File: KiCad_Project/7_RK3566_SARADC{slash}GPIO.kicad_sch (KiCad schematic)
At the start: 9 parts

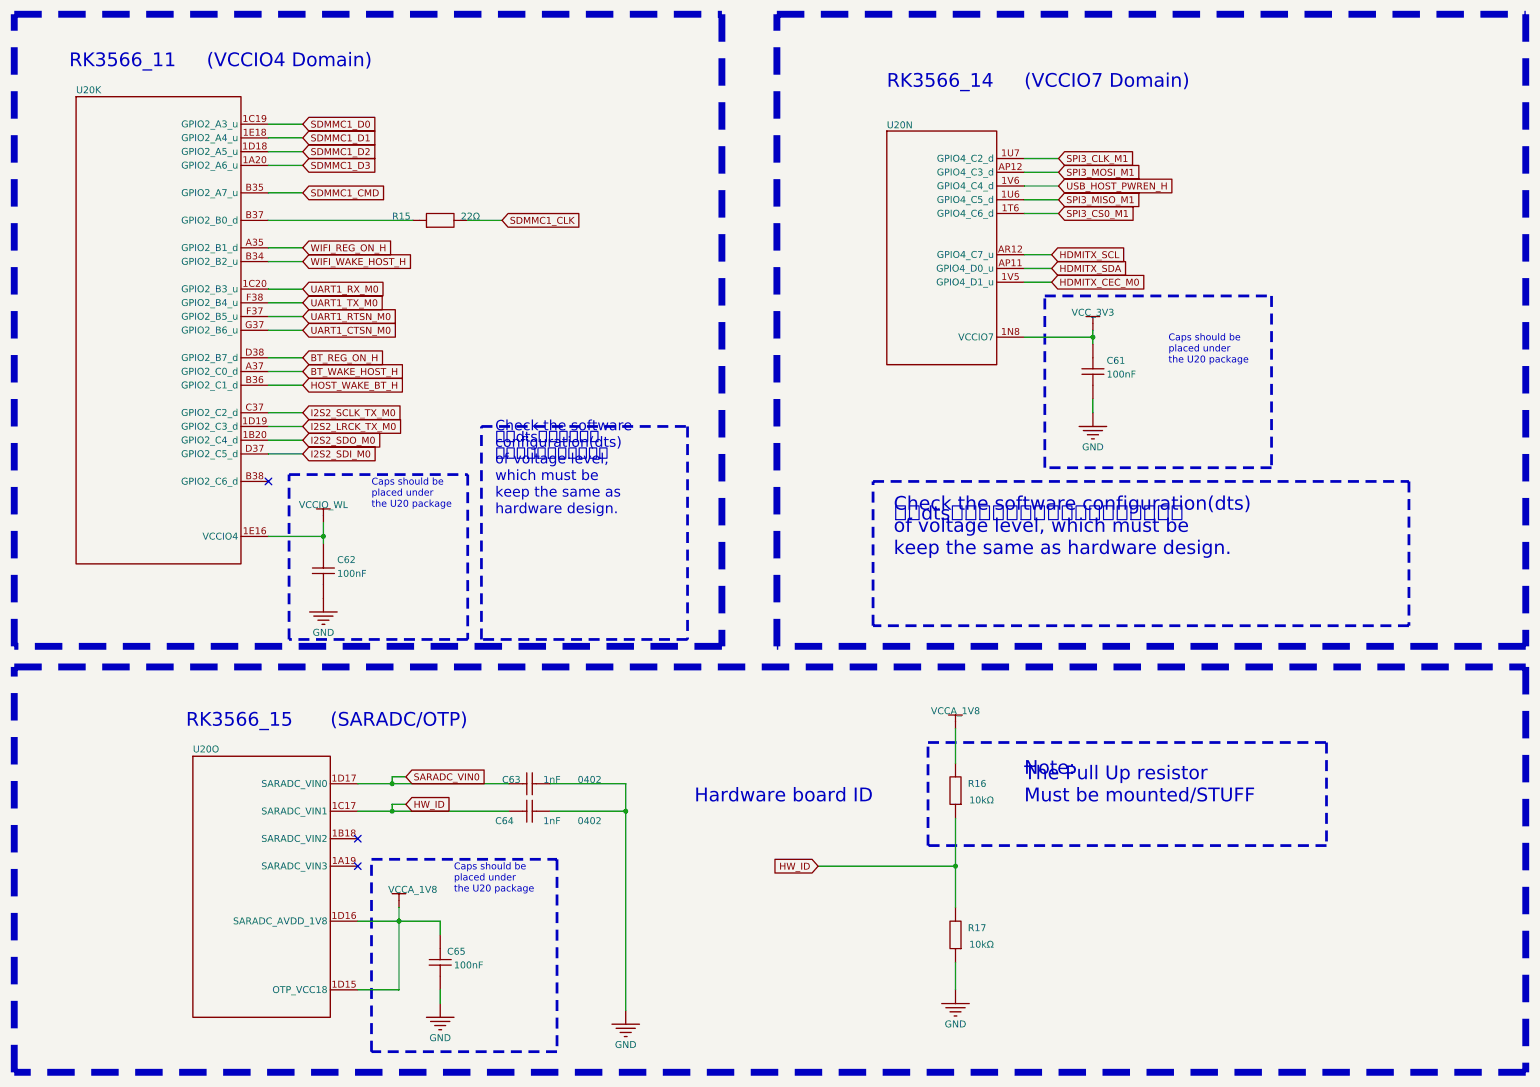
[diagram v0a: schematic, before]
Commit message: Update additional PCBs
Add WIFI PCB to get best antenna
Add Display Debbugger to get interface pinout
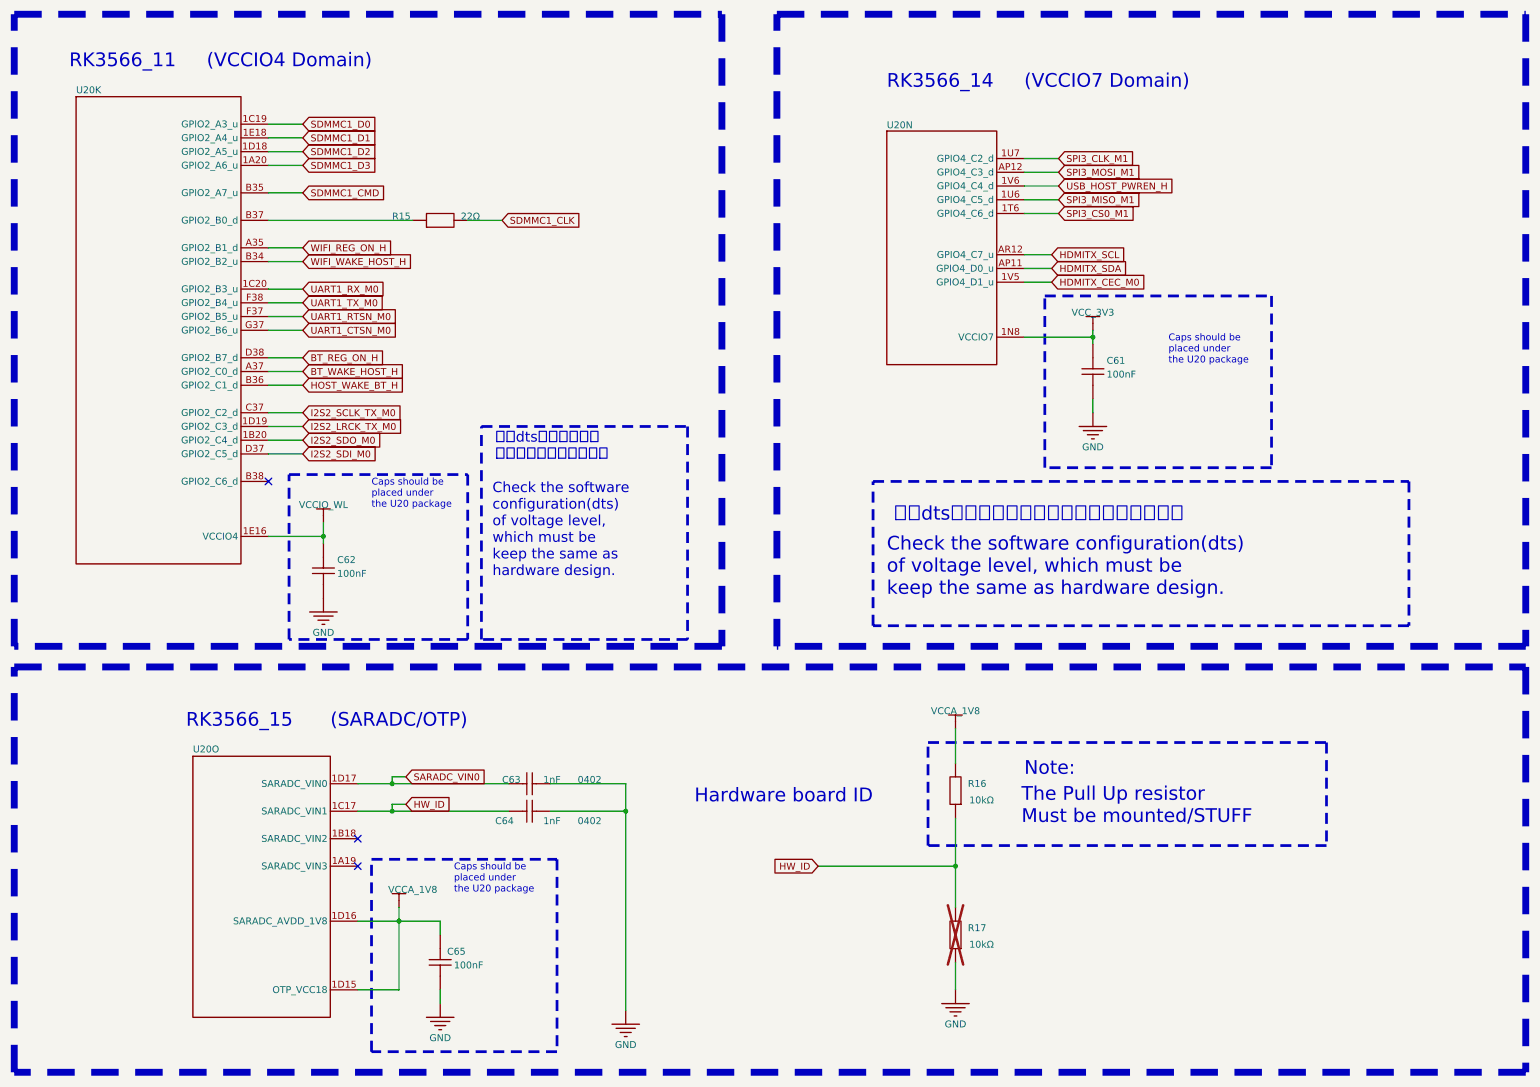
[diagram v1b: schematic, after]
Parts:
- R17: now not fitted; now left out of the parts list
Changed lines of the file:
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@@
 	(text "The Pull Up resistor\nMust be mounted/STUFF"
 		(exclude_from_sim no)
-		(at 255.27 189.23 0)
+		(at 254.762 193.04 0)
 		(effects
 			(font
@@
 	(text "Check the software configuration(dts)\nof voltage level, which must be\nkeep the same as hardware design."
 		(exclude_from_sim no)
-		(at 231.14 143.51 0)
+		(at 229.87 150.876 0)
 		(effects
 			(font
@@
 	(text "Check the software \nconfiguration(dts)\nof voltage level, \nwhich must be\nkeep the same as \nhardware design."
 		(exclude_from_sim no)
-		(at 157.48 135.89 0)
+		(at 156.972 147.32 0)
 		(effects
 			(font
@@
 		(unit 1)
 		(exclude_from_sim no)
-		(in_bom yes)
+		(in_bom no)
 		(on_board yes)
-		(dnp no)
+		(dnp yes)
 		(property "Reference" "R17"
 			(at 244.856 212.8266 90)
